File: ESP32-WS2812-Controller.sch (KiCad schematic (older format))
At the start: 18 parts

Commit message: Annotated schematic and added footprints.
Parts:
- C1: renamed from C?; footprint (none) -> Capacitors_THT:CP_Radial_D5.0mm_P2.50mm
- D1, D2, D3: renamed from D?; footprint (none) -> LEDs:LED_0805
- FB1: renamed from FB?; footprint (none) -> Inductors_SMD:L_0805
- J1: renamed from J?; footprint (none) -> Connectors:USB_Micro-B
- J2: renamed from J?; footprint (none) -> Connectors_Molex:Molex_KK-6410-02_02x2.54mm_Straight
- J3: renamed from J?; footprint (none) -> Pin_Headers:Pin_Header_Angled_1x06_Pitch2.54mm
- J4: renamed from J?; footprint (none) -> Connectors_Molex:Molex_KK-6410-03_03x2.54mm_Straight
- Q1: renamed from Q?; footprint (none) -> TO_SOT_Packages_SMD:SOT-23
- R1, R2: renamed from R?; footprint (none) -> Resistors_SMD:R_0805
- R3: renamed from R?; value 10kR -> 480R; footprint (none) -> Resistors_SMD:R_0805
- R4, R5, R6, R7: renamed from R?; footprint (none) -> Resistors_SMD:R_0603
- SW1: renamed from SW?; footprint (none) -> Buttons_Switches_THT:SW_PUSH-12mm

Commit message: Fixed library symbol for the 3.3V regulator. Also added correct footprint path for the ESP-12F.
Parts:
- J3: footprint Pin_Headers:Pin_Header_Angled_1x06_Pitch2.54mm -> Pin_Headers:Pin_Header_Straight_1x06_Pitch2.54mm
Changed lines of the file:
@@
 F 0 "J3" H 7730 3242 50  0000 L CNN
 F 1 "Conn_01x06" H 7730 3151 50  0000 L CNN
-F 2 "Pin_Headers:Pin_Header_Angled_1x06_Pitch2.54mm" H 7650 3250 50  0001 C CNN
+F 2 "Pin_Headers:Pin_Header_Straight_1x06_Pitch2.54mm" H 7650 3250 50  0001 C CNN
 F 3 "~" H 7650 3250 50  0001 C CNN
 	1    7650 3250

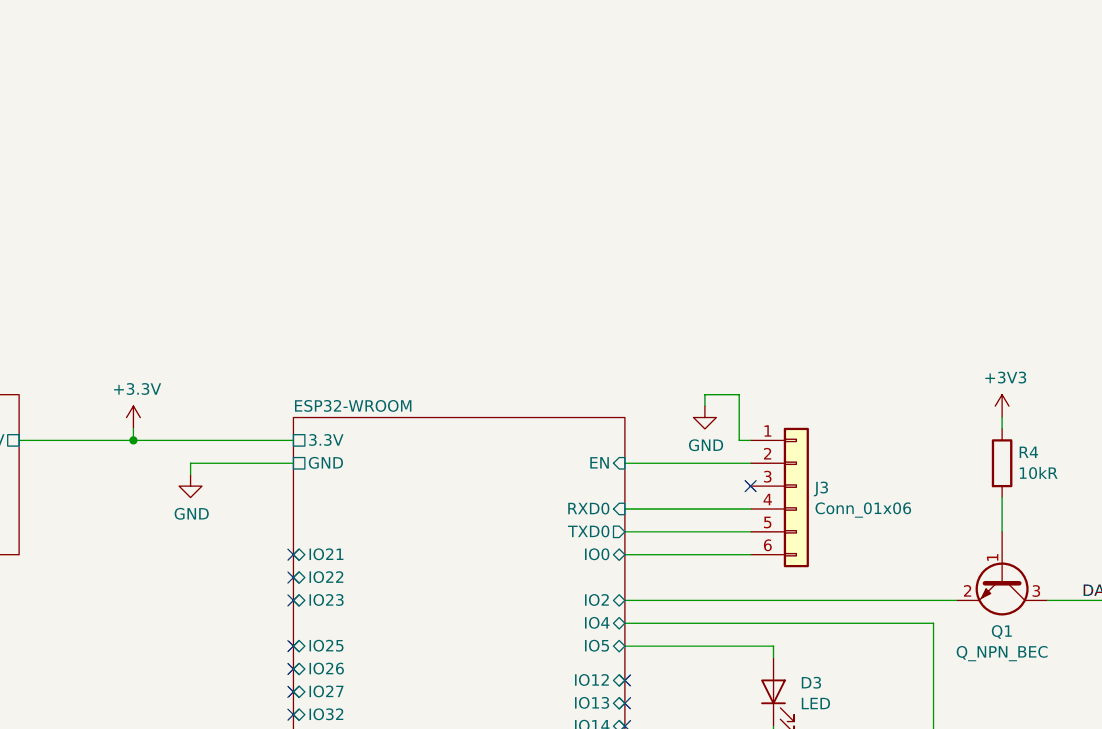
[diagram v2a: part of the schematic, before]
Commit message: Placed components and finished first pass of PCB layout.
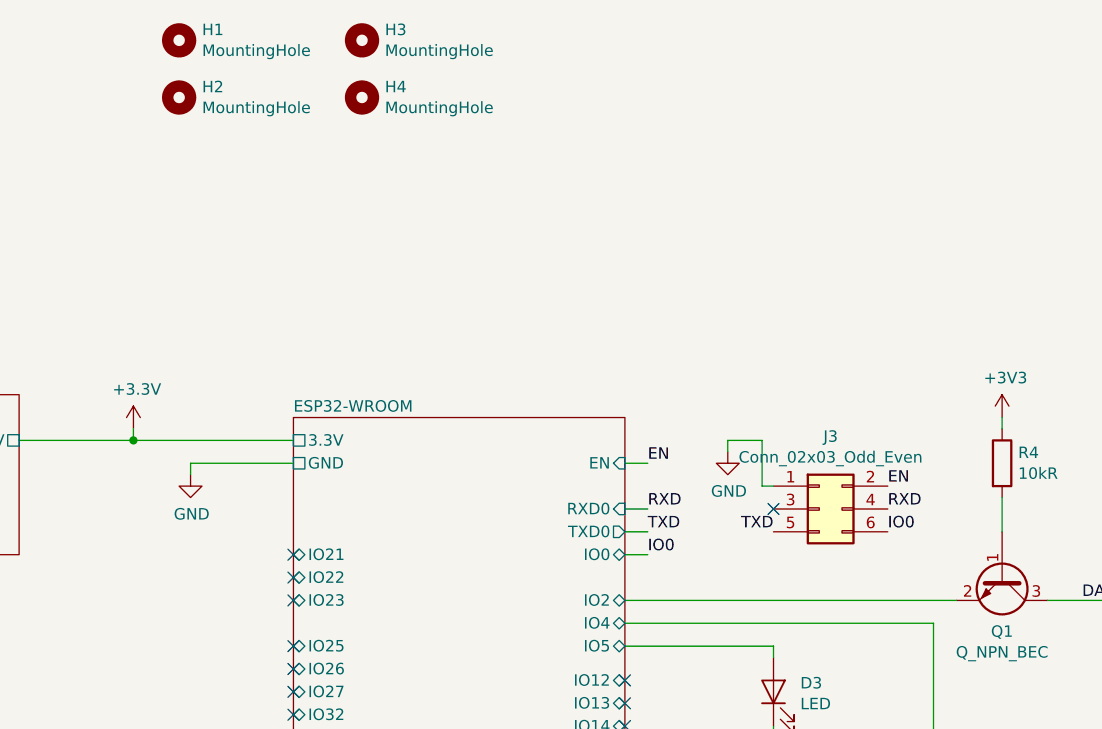
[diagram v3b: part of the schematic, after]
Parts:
- removed J3: Conn_01x06, Pin_Headers:Pin_Header_Straight_1x06_Pitch2.54mm, symbol Connector_Generic:Conn_01x06
- added H1, H2, H3, H4: MountingHole, Mounting_Holes:MountingHole_2.5mm, symbol Mechanical:MountingHole
- added J3: Conn_02x03_Odd_Even, Pin_Headers:Pin_Header_Straight_2x03_Pitch2.54mm, symbol Connector_Generic:Conn_02x03_Odd_Even
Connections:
- net GND: now also J3.1 (Pin_1)
- new net EN: J3.2 (Pin_2)
- new net IO0: J3.6 (Pin_6)
- new net RXD: J3.4 (Pin_4)
- new net TXD: J3.5 (Pin_5)
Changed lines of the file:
@@
 	9300 3350 9300 3400
-$Comp
-L Connector_Generic:Conn_01x06 J3
-U 1 1 5BDAB345
-P 7650 3250
-F 0 "J3" H 7730 3242 50  0000 L CNN
-F 1 "Conn_01x06" H 7730 3151 50  0000 L CNN
-F 2 "Pin_Headers:Pin_Header_Straight_1x06_Pitch2.54mm" H 7650 3250 50  0001 C CNN
-F 3 "~" H 7650 3250 50  0001 C CNN
-	1    7650 3250
-	1    0    0    -1
-$EndComp
-Wire Wire Line
-	6900 3550 7450 3550
-Wire Wire Line
-	7450 3450 6900 3450
-Wire Wire Line
-	7450 3350 6900 3350
-Wire Wire Line
-	7450 3150 6900 3150
 $Comp
 L power:GND #PWR013
 U 1 1 5BDADA2A
-P 7250 2900
-F 0 "#PWR013" H 7250 2650 50  0001 C CNN
-F 1 "GND" H 7255 2727 50  0000 C CNN
-F 2 "" H 7250 2900 50  0001 C CNN
-F 3 "" H 7250 2900 50  0001 C CNN
-	1    7250 2900
-	1    0    0    -1
-$EndComp
-Wire Wire Line
-	7450 3050 7400 3050
-Wire Wire Line
-	7400 3050 7400 2850
-Wire Wire Line
-	7400 2850 7250 2850
-Wire Wire Line
-	7250 2850 7250 2900
-NoConn ~ 7450 3250
+P 7350 3100
+F 0 "#PWR013" H 7350 2850 50  0001 C CNN
+F 1 "GND" H 7355 2927 50  0000 C CNN
+F 2 "" H 7350 3100 50  0001 C CNN
+F 3 "" H 7350 3100 50  0001 C CNN
+	1    7350 3100
+	1    0    0    -1
+$EndComp
+Wire Wire Line
+	7550 3250 7500 3250
+Wire Wire Line
+	7500 3250 7500 3050
+Wire Wire Line
+	7500 3050 7350 3050
+Wire Wire Line
+	7350 3050 7350 3100
+NoConn ~ 7550 3350
 Wire Wire Line
 	8250 4900 8250 3850
@@
 NoConn ~ 6900 4200
 NoConn ~ 6900 4100
+$Comp
+L Mechanical:MountingHole H1
+U 1 1 5BE4D68E
+P 4950 1300
+F 0 "H1" H 5050 1346 50  0000 L CNN
+F 1 "MountingHole" H 5050 1255 50  0000 L CNN
+F 2 "Mounting_Holes:MountingHole_2.5mm" H 4950 1300 50  0001 C CNN
+F 3 "~" H 4950 1300 50  0001 C CNN
+	1    4950 1300
+	1    0    0    -1
+$EndComp
+$Comp
+L Mechanical:MountingHole H2
+U 1 1 5BE4D791
+P 4950 1550
+F 0 "H2" H 5050 1596 50  0000 L CNN
+F 1 "MountingHole" H 5050 1505 50  0000 L CNN
+F 2 "Mounting_Holes:MountingHole_2.5mm" H 4950 1550 50  0001 C CNN
+F 3 "~" H 4950 1550 50  0001 C CNN
+	1    4950 1550
+	1    0    0    -1
+$EndComp
+$Comp
+L Mechanical:MountingHole H3
+U 1 1 5BE4D7EF
+P 5750 1300
+F 0 "H3" H 5850 1346 50  0000 L CNN
+F 1 "MountingHole" H 5850 1255 50  0000 L CNN
+F 2 "Mounting_Holes:MountingHole_2.5mm" H 5750 1300 50  0001 C CNN
+F 3 "~" H 5750 1300 50  0001 C CNN
+	1    5750 1300
+	1    0    0    -1
+$EndComp
+$Comp
+L Mechanical:MountingHole H4
+U 1 1 5BE4D857
+P 5750 1550
+F 0 "H4" H 5850 1596 50  0000 L CNN
+F 1 "MountingHole" H 5850 1505 50  0000 L CNN
+F 2 "Mounting_Holes:MountingHole_2.5mm" H 5750 1550 50  0001 C CNN
+F 3 "~" H 5750 1550 50  0001 C CNN
+	1    5750 1550
+	1    0    0    -1
+$EndComp
+$Comp
+L Connector_Generic:Conn_02x03_Odd_Even J3
+U 1 1 5BE4DF00
+P 7750 3350
+F 0 "J3" H 7800 3667 50  0000 C CNN
+F 1 "Conn_02x03_Odd_Even" H 7800 3576 50  0000 C CNN
+F 2 "Pin_Headers:Pin_Header_Straight_2x03_Pitch2.54mm" H 7750 3350 50  0001 C CNN
+F 3 "~" H 7750 3350 50  0001 C CNN
+	1    7750 3350
+	1    0    0    -1
+$EndComp
+Text Label 7000 3150 0    50   ~ 0
+EN
+Text Label 7000 3350 0    50   ~ 0
+RXD
+Text Label 7000 3450 0    50   ~ 0
+TXD
+Text Label 7000 3550 0    50   ~ 0
+IO0
+Wire Wire Line
+	6900 3150 7000 3150
+Wire Wire Line
+	6900 3350 7000 3350
+Wire Wire Line
+	6900 3450 7000 3450
+Wire Wire Line
+	6900 3550 7000 3550
+Text Label 8050 3250 0    50   ~ 0
+EN
+Text Label 8050 3350 0    50   ~ 0
+RXD
+Text Label 7550 3450 2    50   ~ 0
+TXD
+Text Label 8050 3450 0    50   ~ 0
+IO0
 $EndSCHEMATC

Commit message: Added ADC & power breakout for microphone board
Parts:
- added J5: Conn_01x03, Pin_Headers:Pin_Header_Straight_1x03_Pitch2.54mm, symbol Connector_Generic:Conn_01x03
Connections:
- net +3V3: now also J5.1 (Pin_1)
- net GND: now also J5.2 (Pin_2)
- new net Mic_Input: J5.3 (Pin_3)
- no-connect marks 30 -> 29
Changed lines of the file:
@@
 NoConn ~ 5450 4150
 NoConn ~ 5450 4350
-NoConn ~ 5450 4250
 NoConn ~ 5450 4450
 NoConn ~ 5450 4550
@@
 Text Label 8050 3450 0    50   ~ 0
 IO0
+$Comp
+L Connector_Generic:Conn_01x03 J5
+U 1 1 5BE8BF84
+P 4550 4000
+F 0 "J5" H 4470 4317 50  0000 C CNN
+F 1 "Conn_01x03" H 4470 4226 50  0000 C CNN
+F 2 "Pin_Headers:Pin_Header_Straight_1x03_Pitch2.54mm" H 4550 4000 50  0001 C CNN
+F 3 "~" H 4550 4000 50  0001 C CNN
+	1    4550 4000
+	-1   0    0    -1
+$EndComp
+$Comp
+L power:+3V3 #PWR021
+U 1 1 5BE8C06A
+P 5000 3900
+F 0 "#PWR021" H 5000 3750 50  0001 C CNN
+F 1 "+3V3" H 5015 4073 50  0000 C CNN
+F 2 "" H 5000 3900 50  0001 C CNN
+F 3 "" H 5000 3900 50  0001 C CNN
+	1    5000 3900
+	1    0    0    -1
+$EndComp
+$Comp
+L power:GND #PWR022
+U 1 1 5BE8C13E
+P 5100 4000
+F 0 "#PWR022" H 5100 3750 50  0001 C CNN
+F 1 "GND" H 5105 3827 50  0000 C CNN
+F 2 "" H 5100 4000 50  0001 C CNN
+F 3 "" H 5100 4000 50  0001 C CNN
+	1    5100 4000
+	1    0    0    -1
+$EndComp
+Wire Wire Line
+	5450 4250 4950 4250
+Wire Wire Line
+	4950 4250 4950 4100
+Text Label 4950 4250 2    50   ~ 0
+Mic_Input
+Wire Wire Line
+	4750 4100 4950 4100
+Wire Wire Line
+	4750 4000 5100 4000
+Wire Wire Line
+	4750 3900 5000 3900
 $EndSCHEMATC
